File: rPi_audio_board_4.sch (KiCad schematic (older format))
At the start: 57 parts, among them P4 9V DC, U2 74HC125

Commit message: uploaded
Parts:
- removed C1: 100n, symbol C
- removed D?: DIODE, symbol DIODE
- removed MIDI~IN: DIN_5, symbol DIN_5
- removed R1, R2: 220, symbol R
- removed U2: 74HC125, symbol 74LS125
- removed U?: U1 Opto, symbol OPTO_DARLINGTON
- removed rPi~P1~Header: GPIO header, symbol CONN_13X2
- added J1: RASPI_IO_HEADER, symbol RASPI_IO_HEADER
- J3: renamed from P?; value HEADER_8 -> PIN OUT
- L1, L2: renamed from 10uH; value INDUCTOR -> 10uH
- P4: renamed from P?; value HEADER2 -> LINE IN
- P5: renamed from P?; value HEADER_6D -> MODE SET
- gave numbers to parts that had none: 42
- renumbered rPi~P5~header to J2, P4 to P1
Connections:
- net labels added: DC IN
- net labels removed: 9VDC
- wire segments 180 -> 169
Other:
- note added: "SMd poarts sizes: 0805 seems standard for resistors. Try this for caps too and inductors if possible.\n"
- moved on the sheet: C1, C10, C11, C12, C13, C14, C15, C16, C17, C18, C19, C2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

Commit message: shcematic update
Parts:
- removed U7: DRV135, MODULE, symbol DRV135
- added R?: 10k, symbol R
- added U?: DRV135, MODULE, symbol DRV135
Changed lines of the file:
@@
 LIBS:valves
 LIBS:w_vacuum
+LIBS:Paspu_IO_Header
 LIBS:w_analog
 LIBS:w_connectors
@@
 LIBS:w_rtx
 LIBS:w_transistor
-LIBS:rPi_audio_board_4_no_MIDI-cache
+LIBS:MIC5207BM5
+LIBS:MIC5225
+LIBS:MIC39100-5.0
+LIBS:PLL1705
+LIBS:PLL1705 (1)
+LIBS:WM8731
+LIBS:rPi_audio_board_4-cache
 EELAYER 24 0
 EELAYER END
@@
 Text GLabel 14000 3100 3    60   Input ~ 0
 +9VDC
-$Comp
-L DRV135 U7
-U 1 1 5202A658
-P 14250 1950
-F 0 "U7" H 14250 1850 50  0000 C CNN
-F 1 "DRV135" H 14250 2050 50  0000 C CNN
-F 2 "MODULE" H 14250 1950 50  0001 C CNN
-F 3 "DOCUMENTATION" H 14250 1950 50  0001 C CNN
-	1    14250 1950
-	1    0    0    -1
-$EndComp
 Text GLabel 13250 2250 0    60   Input ~ 0
 VREF
@@
 Wire Wire Line
 	10100 5850 8300 5850
-Wire Wire Line
-	7900 1800 7450 1800
 Wire Wire Line
 	12200 6350 13250 6350
@@
 Text Notes 3500 9050 0    60   ~ 0
 SMd poarts sizes: 0805 seems standard for resistors. Try this for caps too and inductors if possible.\n
+$Comp
+L DRV135 U?
+U 1 1 5206F205
+P 14250 1950
+F 0 "U?" H 14250 1850 50  0000 C CNN
+F 1 "DRV135" H 14250 2050 50  0000 C CNN
+F 2 "MODULE" H 14250 1950 50  0001 C CNN
+F 3 "DOCUMENTATION" H 14250 1950 50  0001 C CNN
+	1    14250 1950
+	1    0    0    -1
+$EndComp
+$Comp
+L R R?
+U 1 1 5206F38F
+P 7700 1800
+F 0 "R?" V 7780 1800 40  0000 C CNN
+F 1 "10k" V 7707 1801 40  0000 C CNN
+F 2 "" V 7630 1800 30  0000 C CNN
+F 3 "" H 7700 1800 30  0000 C CNN
+	1    7700 1800
+	0    -1   -1   0
+$EndComp
+Text GLabel 8000 1800 2    60   Input ~ 0
++5VDC
+Wire Wire Line
+	7950 1800 8000 1800
+Connection ~ 7950 1800
 $EndSCHEMATC

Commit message: schematic development
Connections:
- wire segments 169 -> 170
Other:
- moved on the sheet: C2, C6
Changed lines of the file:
@@
 EESchema Schematic File Version 2
+LIBS:rPi_audio_board_4-cache
+LIBS:device
 LIBS:power
-LIBS:device
-LIBS:transistors
-LIBS:conn
-LIBS:linear
-LIBS:regul
-LIBS:74xx
-LIBS:cmos4000
-LIBS:adc-dac
-LIBS:memory
-LIBS:xilinx
-LIBS:special
-LIBS:microcontrollers
-LIBS:dsp
-LIBS:microchip
-LIBS:analog_switches
-LIBS:motorola
-LIBS:texas
-LIBS:intel
-LIBS:audio
-LIBS:interface
-LIBS:digital-audio
-LIBS:philips
-LIBS:display
-LIBS:cypress
-LIBS:siliconi
-LIBS:opto
-LIBS:atmel
-LIBS:contrib
-LIBS:valves
-LIBS:w_vacuum
-LIBS:Paspu_IO_Header
 LIBS:w_analog
 LIBS:w_connectors
@@
 LIBS:w_rtx
 LIBS:w_transistor
-LIBS:MIC5207BM5
-LIBS:MIC5225
-LIBS:MIC39100-5.0
-LIBS:PLL1705
-LIBS:PLL1705 (1)
-LIBS:WM8731
+LIBS:w_vacuum
 LIBS:rPi_audio_board_4-cache
 EELAYER 24 0
@@
 Text GLabel 1400 1300 0    60   Output ~ 0
 I2C_SDA
-Text GLabel 4850 7200 2    60   Output ~ 0
+Text GLabel 4900 7150 2    60   Output ~ 0
 +3.3VDC
 Text GLabel 3250 1200 2    60   Input ~ 0
@@
 L C C6
 U 1 1 5200CE14
-P 4300 7400
-F 0 "C6" H 4350 7500 50  0000 L CNN
-F 1 "2.2uF" H 4350 7300 50  0000 L CNN
-F 2 "" H 4300 7400 60  0000 C CNN
-F 3 "" H 4300 7400 60  0000 C CNN
-	1    4300 7400
+P 4300 7350
+F 0 "C6" H 4350 7450 50  0000 L CNN
+F 1 "2.2uF" H 4350 7250 50  0000 L CNN
+F 2 "" H 4300 7350 60  0000 C CNN
+F 3 "" H 4300 7350 60  0000 C CNN
+	1    4300 7350
 	1    0    0    -1
 $EndComp
@@
 L C C2
 U 1 1 5200CE26
-P 2400 7350
-F 0 "C2" H 2450 7450 50  0000 L CNN
-F 1 "1.0uF" H 2450 7250 50  0000 L CNN
-F 2 "" H 2400 7350 60  0000 C CNN
-F 3 "" H 2400 7350 60  0000 C CNN
-	1    2400 7350
-	1    0    0    -1
-$EndComp
-Text GLabel 3000 8000 0    60   Input ~ 0
+P 2400 7450
+F 0 "C2" H 2450 7550 50  0000 L CNN
+F 1 "1.0uF" H 2450 7350 50  0000 L CNN
+F 2 "" H 2400 7450 60  0000 C CNN
+F 3 "" H 2400 7450 60  0000 C CNN
+	1    2400 7450
+	1    0    0    -1
+$EndComp
+Text GLabel 3150 6800 0    60   Input ~ 0
 GPIO4
 Text GLabel 1300 1500 0    60   BiDi ~ 0
@@
 P 3350 7400
 F 0 "U3" H 3000 7750 50  0000 C CNN
-F 1 "MIC5225" H 3350 7600 50  0000 C CNN
+F 1 "MIC5225" H 3350 7400 50  0000 C CNN
 F 2 "MODULE" H 3350 7400 50  0001 C CNN
 F 3 "DOCUMENTATION" H 3350 7400 50  0001 C CNN
@@
 	12200 5750 14800 5750
 Wire Wire Line
-	4100 7200 4850 7200
-Connection ~ 4300 7200
+	4100 7150 4900 7150
+Connection ~ 4300 7150
 Wire Wire Line
 	1800 7800 4300 7800
@@
 Wire Wire Line
 	4650 1700 4700 1700
-Connection ~ 2400 7550
+Connection ~ 2400 7650
 Connection ~ 2400 7150
-Connection ~ 3200 8000
-Connection ~ 2600 7550
-Wire Wire Line
-	4300 7800 4300 7600
-Connection ~ 4300 7600
+Connection ~ 3350 6800
+Connection ~ 2600 7650
 Connection ~ 4050 6000
 Wire Wire Line
@@
 	2250 7150 2600 7150
 Wire Wire Line
-	2400 7550 2400 7800
-Connection ~ 2400 7800
-Wire Wire Line
-	2600 7550 2400 7550
-Wire Wire Line
-	3000 8000 3200 8000
+	2400 7800 2400 7650
+Wire Wire Line
+	2400 7650 2600 7650
+Wire Wire Line
+	3150 6800 3350 6800
 $Comp
 L RASPI_IO_HEADER J1
@@
 	7950 1800 8000 1800
 Connection ~ 7950 1800
+Wire Wire Line
+	2400 7150 2400 7250
+Connection ~ 2400 7250
+Connection ~ 4300 7550
+Wire Wire Line
+	4300 7800 4300 7550
+Connection ~ 2400 7800
 $EndSCHEMATC

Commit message: started on rough board layout
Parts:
- gave numbers to parts that had none: 2
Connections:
- wire segments 170 -> 167
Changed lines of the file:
@@
 DVDD
 $Comp
-L AGND #PWR9
+L AGND #PWR01
 U 1 1 51D91263
 P 12350 7650
-F 0 "#PWR9" H 12350 7650 40  0001 C CNN
+F 0 "#PWR01" H 12350 7650 40  0001 C CNN
 F 1 "AGND" H 12350 7580 50  0000 C CNN
 F 2 "" H 12350 7650 60  0001 C CNN
@@
 +9VDC
 $Comp
-L GNDPWR #PWR4
+L GNDPWR #PWR02
 U 1 1 51CFF2E2
 P 2050 10550
-F 0 "#PWR4" H 2050 10600 40  0001 C CNN
+F 0 "#PWR02" H 2050 10600 40  0001 C CNN
 F 1 "GNDPWR" H 2050 10450 40  0000 C CNN
 F 2 "" H 2050 10550 60  0001 C CNN
@@
 $EndComp
 $Comp
-L AGND #PWR7
+L AGND #PWR03
 U 1 1 52023752
 P 8750 10600
-F 0 "#PWR7" H 8750 10600 40  0001 C CNN
+F 0 "#PWR03" H 8750 10600 40  0001 C CNN
 F 1 "AGND" H 8750 10530 50  0000 C CNN
 F 2 "" H 8750 10600 60  0000 C CNN
@@
 VREF
 $Comp
-L AGND #PWR8
+L AGND #PWR04
 U 1 1 52023E4B
 P 11250 3100
-F 0 "#PWR8" H 11250 3100 40  0001 C CNN
+F 0 "#PWR04" H 11250 3100 40  0001 C CNN
 F 1 "AGND" H 11250 3030 50  0000 C CNN
 F 2 "" H 11250 3100 60  0000 C CNN
@@
 VREF
 $Comp
-L AGND #PWR10
+L AGND #PWR05
 U 1 1 5202A65F
 P 14500 3100
-F 0 "#PWR10" H 14500 3100 40  0001 C CNN
+F 0 "#PWR05" H 14500 3100 40  0001 C CNN
 F 1 "AGND" H 14500 3030 50  0000 C CNN
 F 2 "" H 14500 3100 60  0000 C CNN
@@
 Connection ~ 3250 2100
 Wire Wire Line
-	3250 2600 3250 1400
+	3250 1400 3250 2600
 Connection ~ 3250 1800
 Wire Wire Line
@@
 	4550 1900 4550 2150
 $Comp
-L DGND #PWR6
+L DGND #PWR06
 U 1 1 5204665C
 P 4550 2150
-F 0 "#PWR6" H 4550 2150 40  0001 C CNN
+F 0 "#PWR06" H 4550 2150 40  0001 C CNN
 F 1 "DGND" H 4550 2080 40  0000 C CNN
 F 2 "" H 4550 2150 60  0000 C CNN
@@
 	1300 1600 1300 2750
 $Comp
-L DGND #PWR1
+L DGND #PWR07
 U 1 1 52046AB5
 P 1300 2750
-F 0 "#PWR1" H 1300 2750 40  0001 C CNN
+F 0 "#PWR07" H 1300 2750 40  0001 C CNN
 F 1 "DGND" H 1300 2680 40  0000 C CNN
 F 2 "" H 1300 2750 60  0000 C CNN
@@
 	1800 5150 1800 7950
 $Comp
-L AGND #PWR3
+L AGND #PWR08
 U 1 1 52047368
 P 1800 7950
-F 0 "#PWR3" H 1800 7950 40  0001 C CNN
+F 0 "#PWR08" H 1800 7950 40  0001 C CNN
 F 1 "AGND" H 1800 7880 50  0000 C CNN
 F 2 "" H 1800 7950 60  0000 C CNN
@@
 Wire Wire Line
 	3250 1400 3050 1400
-$Comp
-L AGND #PWR5
-U 1 1 52059EC0
-P 2400 10550
-F 0 "#PWR5" H 2400 10550 40  0001 C CNN
-F 1 "AGND" H 2400 10480 50  0000 C CNN
-F 2 "" H 2400 10550 60  0000 C CNN
-F 3 "" H 2400 10550 60  0000 C CNN
-	1    2400 10550
-	1    0    0    -1
-$EndComp
-$Comp
-L DGND #PWR2
-U 1 1 52059ED4
-P 1750 10550
-F 0 "#PWR2" H 1750 10550 40  0001 C CNN
-F 1 "DGND" H 1750 10480 40  0000 C CNN
-F 2 "" H 1750 10550 60  0000 C CNN
-F 3 "" H 1750 10550 60  0000 C CNN
-	1    1750 10550
-	1    0    0    -1
-$EndComp
-Wire Wire Line
-	1750 10300 2400 10300
-Wire Wire Line
-	1750 10300 1750 10550
 Connection ~ 2050 10300
-Wire Wire Line
-	2400 10300 2400 10550
 Text Notes 3500 9050 0    60   ~ 0
 SMd poarts sizes: 0805 seems standard for resistors. Try this for caps too and inductors if possible.\n
 $Comp
-L DRV135 U?
+L DRV135 U7
 U 1 1 5206F205
 P 14250 1950
-F 0 "U?" H 14250 1850 50  0000 C CNN
+F 0 "U7" H 14250 1850 50  0000 C CNN
 F 1 "DRV135" H 14250 2050 50  0000 C CNN
 F 2 "MODULE" H 14250 1950 50  0001 C CNN
@@
 $EndComp
 $Comp
-L R R?
+L R R13
 U 1 1 5206F38F
 P 7700 1800
-F 0 "R?" V 7780 1800 40  0000 C CNN
+F 0 "R13" V 7780 1800 40  0000 C CNN
 F 1 "10k" V 7707 1801 40  0000 C CNN
 F 2 "" V 7630 1800 30  0000 C CNN
@@
 	4300 7800 4300 7550
 Connection ~ 2400 7800
+Text HLabel 10000 9500 2    60   Output ~ 0
+LHPOUT
+Wire Bus Line
+	10000 9500 9550 9500
+Text HLabel 10000 9700 2    60   Output ~ 0
+RHPOUT
+Wire Bus Line
+	10000 9700 9550 9700
 $EndSCHEMATC

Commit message: board development, tidy up gnd etc
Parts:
- removed P3: Output Left, symbol CONNECTOR_2
- removed P4: LINE IN, ~, symbol HEADER2
- removed P6: Output Right, symbol CONNECTOR_2
- removed R13: 10k, symbol R
- added P3, P4, P6: CONNECTOR_3, symbol CONNECTOR_3
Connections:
- wire segments 167 -> 169
- no-connect marks 0 -> 2
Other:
- moved on the sheet: C8, C9, R3, R4

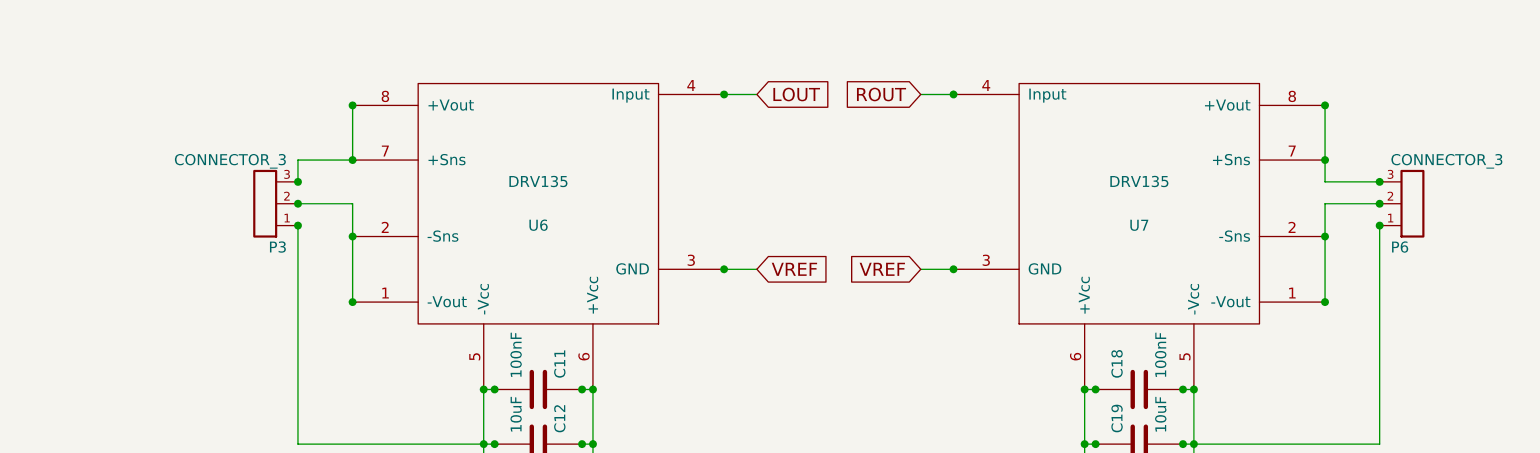
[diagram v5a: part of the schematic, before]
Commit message: refined folder for size
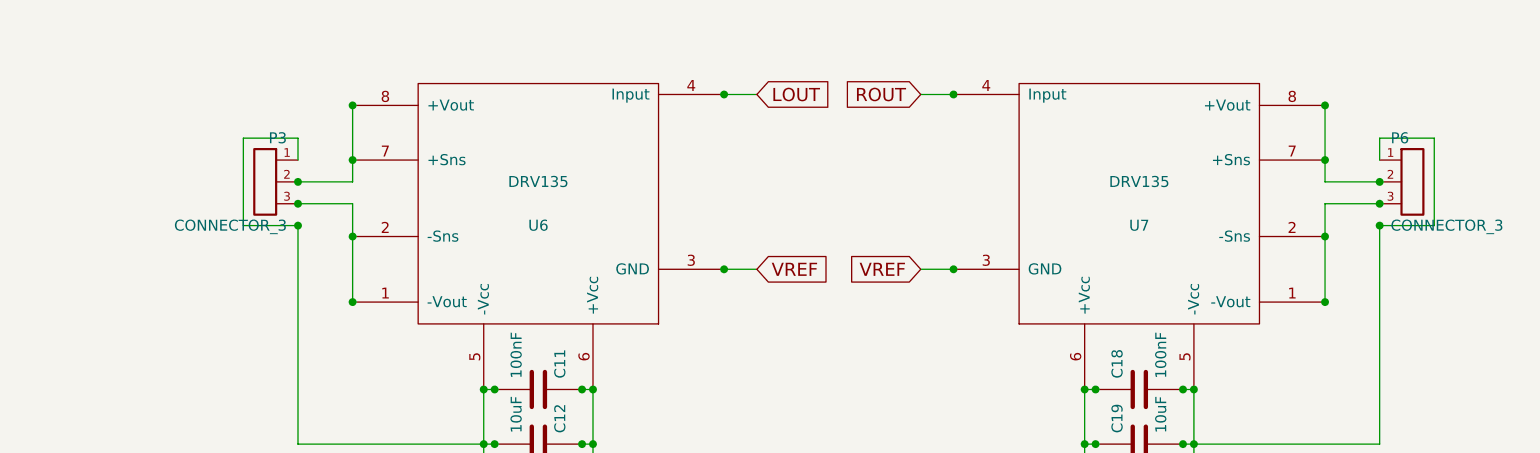
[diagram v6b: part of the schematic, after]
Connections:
- wire segments 169 -> 176
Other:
- moved on the sheet: P3, P6
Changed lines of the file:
@@
 EESchema Schematic File Version 2
-LIBS:rPi_audio_board_4-cache
-LIBS:w_vacuum
-LIBS:device
-LIBS:w_analog
-LIBS:w_connectors
-LIBS:w_device
-LIBS:w_logic
-LIBS:w_memory
-LIBS:w_microcontrollers
-LIBS:w_opto
-LIBS:w_relay
-LIBS:w_rtx
-LIBS:w_transistor
-LIBS:power
 LIBS:rPi_audio_board_4-cache
 EELAYER 24 0
@@
 	12350 1450 12500 1450
 Wire Wire Line
-	10650 1500 10650 1750
+	10650 1500 10650 1850
 Wire Wire Line
 	10650 1950 10650 2400
-Wire Wire Line
-	10650 1750 10400 1750
-Wire Wire Line
-	10400 1750 10400 1850
 Wire Wire Line
 	11750 2800 11750 3100
@@
 L CONNECTOR_3 P6
 U 1 1 5208BF69
-P 15400 1950
-F 0 "P6" H 15400 2150 50  0000 L CNN
-F 1 "CONNECTOR_3" H 15400 1750 50  0000 L CNN
-F 2 "" H 15400 1950 60  0000 C CNN
-F 3 "" H 15400 1950 60  0000 C CNN
-	1    15400 1950
-	1    0    0    1
+P 15400 1850
+F 0 "P6" H 15400 2050 50  0000 L CNN
+F 1 "CONNECTOR_3" H 15400 1650 50  0000 L CNN
+F 2 "" H 15400 1850 60  0000 C CNN
+F 3 "" H 15400 1850 60  0000 C CNN
+	1    15400 1850
+	1    0    0    -1
 $EndComp
 Wire Wire Line
@@
 L CONNECTOR_3 P3
 U 1 1 5208C698
-P 10350 1950
-F 0 "P3" H 10350 2150 50  0000 L CNN
-F 1 "CONNECTOR_3" H 10350 1750 50  0000 L CNN
-F 2 "" H 10350 1950 60  0000 C CNN
-F 3 "" H 10350 1950 60  0000 C CNN
-	1    10350 1950
-	-1   0    0    1
+P 10350 1850
+F 0 "P3" H 10350 2050 50  0000 L CNN
+F 1 "CONNECTOR_3" H 10350 1650 50  0000 L CNN
+F 2 "" H 10350 1850 60  0000 C CNN
+F 3 "" H 10350 1850 60  0000 C CNN
+	1    10350 1850
+	-1   0    0    -1
 $EndComp
 Wire Wire Line
@@
 NoConn ~ 12200 6750
 NoConn ~ 12200 6850
+Wire Wire Line
+	15350 1750 15350 1650
+Wire Wire Line
+	15350 1650 15600 1650
+Wire Wire Line
+	15600 1650 15600 2050
+Wire Wire Line
+	15600 2050 15350 2050
+Wire Wire Line
+	10650 1850 10400 1850
+Wire Wire Line
+	10400 1750 10400 1650
+Wire Wire Line
+	10400 1650 10150 1650
+Wire Wire Line
+	10150 1650 10150 2050
+Wire Wire Line
+	10150 2050 10400 2050
 $EndSCHEMATC
